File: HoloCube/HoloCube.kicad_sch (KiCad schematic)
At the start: 38 parts, among them J1 ESPProgUART_RX, J2 Conn_01x08_MountingPin, J3 USB_C_Receptacle_USB2.0, J4 Micro_SD_Card, Q1 MMBT3904, U1 ESP32-PICO-D4, U2 LIS2DH12TR, U3 BH1750FVI-TR, U4 XC6209

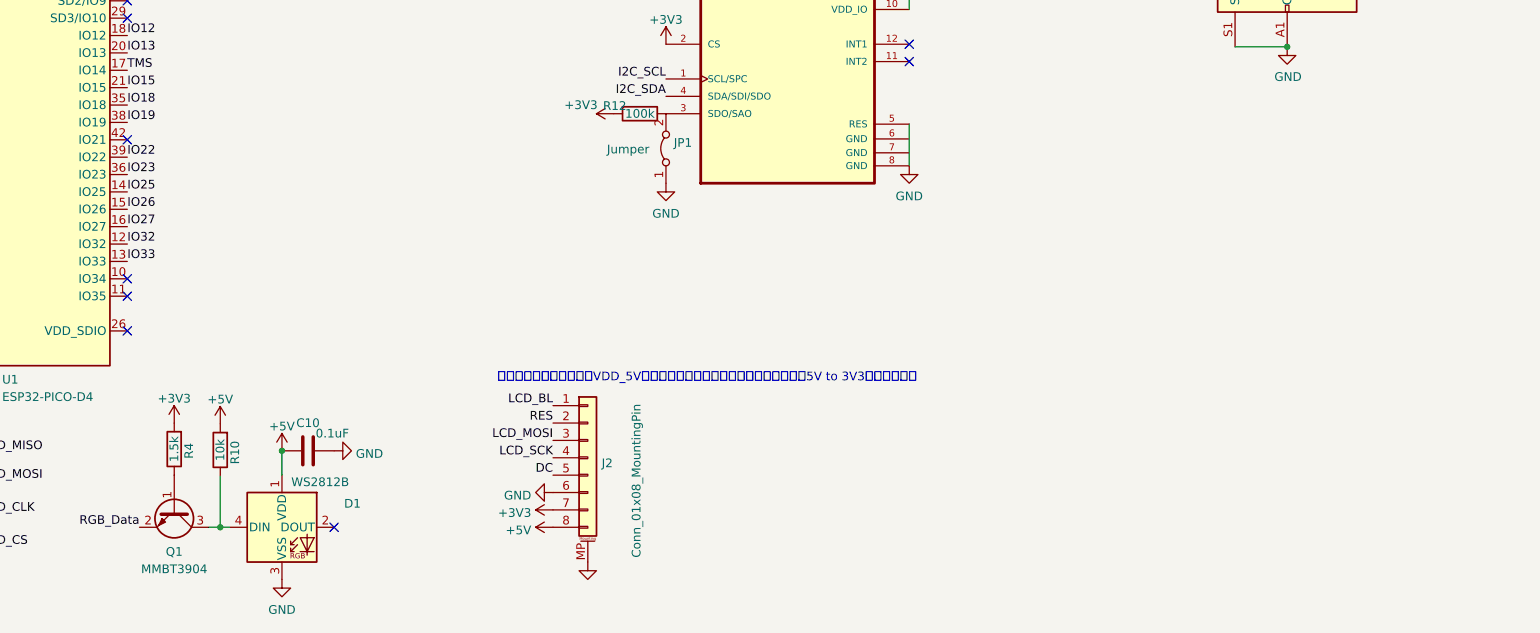
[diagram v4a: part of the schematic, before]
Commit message: 只用三轴还是不方便输入，考虑增加波轮
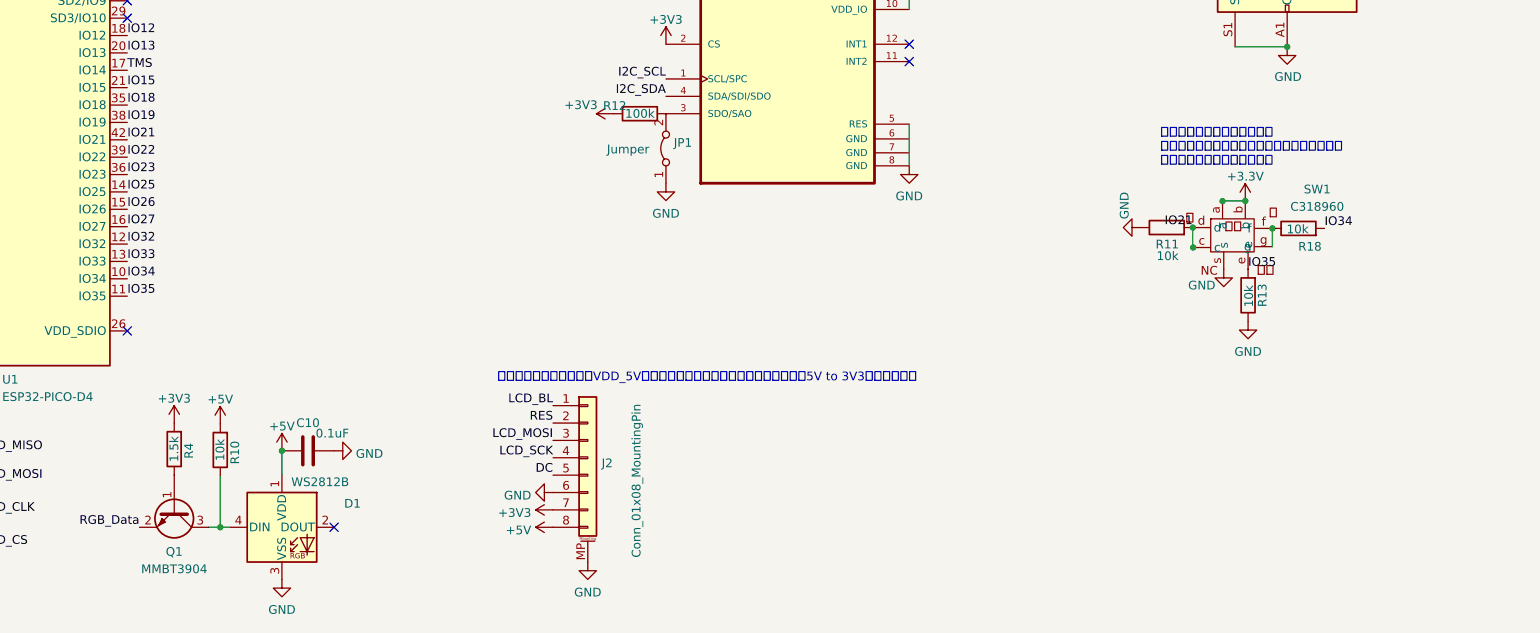
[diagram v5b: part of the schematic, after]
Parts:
- added R11, R13, R18: 10k, Resistor_SMD:R_0402_1005Metric, symbol Device:R
- added SW1: C318960, KisonNew:C318960, symbol KisonNew:C318960
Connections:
- net +3V3: now also SW1.a, SW1.b
- net GND: now also R11.1, R13.1, SW1.s
- net IO34: now reaches U1.10 (IO34)
- net IO34: now also R18.2
- net IO35: now reaches U1.11 (IO35)
- net IO35: now also R13.2, SW1.e
- net IO21: now reaches U1.42 (IO21)
- net IO21: now also SW1.c
- new net: R11.2, SW1.d
- new net: R18.1, SW1.f, SW1.g
- no-connect marks 28 -> 25
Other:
- note added: "这个太丑了，得弄好看一点。 另外如果主板放不下考虑放到屏幕那块板子上？ 其实就应该直接放在屏幕板上"

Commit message: Fix  Error & add SW
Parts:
- removed J2: Conn_01x08_MountingPin, Connector_FFC-FPC:TE_0-1734839-8_1x08-1MP_P0.5mm_Horizontal, symbol Connector_Generic_MountingPin:Conn_01x08_MountingPin
- removed R11, R13, R18: 10k, Resistor_SMD:R_0402_1005Metric, symbol Device:R
- removed R2: 0, Resistor_SMD:R_0402_1005Metric, symbol Device:R
- removed SW1: C318960, KisonNew:C318960, symbol KisonNew:C318960
- added J2: Conn_01x12_MountingPin, Connector_FFC-FPC:Hirose_FH12-12S-0.5SH_1x12-1MP_P0.50mm_Horizontal, symbol Connector_Generic_MountingPin:Conn_01x12_MountingPin
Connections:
- net +3V3: now also J1.2 (VDD), J2.7 (Pin_7)
- net +5V: now also J2.8 (Pin_8)
- net DC: now also J2.5 (Pin_5)
- net GND: now also U2.6 (GND), U2.7 (GND), J2.12 (Pin_12), J2.6 (Pin_6), J2.MP (MountPin)
- net IO18: now also J2.4 (Pin_4)
- net IO22: now also J2.1 (Pin_1)
- net IO4: now also J2.2 (Pin_2)
- net IO5: now also J2.3 (Pin_3)
- net IO12: no longer names the net of U1.18 (IO12)
- net IO21 renamed BTN_Down
- net BTN_Down: now also J2.11 (Pin_11)
- net IO27 renamed BTN_Right
- net BTN_Right: now also J2.9 (Pin_9)
- net TMS renamed BTN_Left
- net BTN_Left: now also J2.10 (Pin_10)
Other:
- note removed: "智慧君的扩展板上，这个VDD_5V其实没用到，可以考虑扩展板上放个额外的5V to 3V3继续降低发热"
- note removed: "这个太丑了，得弄好看一点。 另外如果主板放不下考虑放到屏幕那块板子上？ 其实就应该直接放在屏幕板上"

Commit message: 投板版本
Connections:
- net IO34: no longer names the net of U1.10 (IO34)
- net IO35: no longer names the net of U1.11 (IO35)
- no-connect marks 25 -> 28
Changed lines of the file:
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@@
   (junction (at 45.085 164.084) (diameter 0) (color 0 0 0 0)
   )
+  (no_connect (at 72.898 138.684))
+  (no_connect (at 72.898 141.224))
   (no_connect (at 72.898 98.044))
   (no_connect (at 72.898 100.584))
@@
   (no_connect (at 187.198 104.394))
   (no_connect (at 187.198 106.934))
+  (no_connect (at 72.898 103.124))
   (no_connect (at 103.124 175.006))
   (no_connect (at 228.473 41.148))
@@
     (effects (font (size 1.27 1.27)) (justify left bottom))
   )
-  (label "IO35" (at 72.898 141.224 0)
-    (effects (font (size 1.27 1.27)) (justify left bottom))
-  )
   (label "DC" (at 26.924 173.736 0)
     (effects (font (size 1.27 1.27)) (justify left bottom))
@@
     (effects (font (size 1.27 1.27)) (justify left bottom))
   )
-  (label "IO34" (at 72.898 138.684 0)
-    (effects (font (size 1.27 1.27)) (justify left bottom))
-  )

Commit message: Fix most 3D parts
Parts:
- J2: footprint Connector_FFC-FPC:Hirose_FH12-12S-0.5SH_1x12-1MP_P0.50mm_Horizontal -> KisonNew:Hirose_FH12-12S-0.5SH_1x12-1MP_P0.50mm_Horizontal
- J3: footprint Connector_USB:USB_C_Receptacle_HRO_TYPE-C-31-M-12 -> KisonNew:USB_C_Receptacle_HRO_TYPE-C-31-M-12
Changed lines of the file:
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@@
       (effects (font (size 1.27 1.27)) (justify left))
     )
-    (property "Footprint" "Connector_FFC-FPC:Hirose_FH12-12S-0.5SH_1x12-1MP_P0.50mm_Horizontal" (id 2) (at 149.352 155.956 0)
+    (property "Footprint" "KisonNew:Hirose_FH12-12S-0.5SH_1x12-1MP_P0.50mm_Horizontal" (id 2) (at 149.352 155.956 0)
       (effects (font (size 1.27 1.27)) hide)
     )
@@
     (property "Reference" "J3" (id 0) (at 245.1608 59.8932 0))
     (property "Value" "USB_C_Receptacle_USB2.0" (id 1) (at 244.729 62.484 0))
-    (property "Footprint" "Connector_USB:USB_C_Receptacle_HRO_TYPE-C-31-M-12" (id 2) (at 246.253 81.915 0)
+    (property "Footprint" "KisonNew:USB_C_Receptacle_HRO_TYPE-C-31-M-12" (id 2) (at 246.253 81.915 0)
       (effects (font (size 1.27 1.27)) hide)
     )
@@
     )
     (path "/504ab751-c266-4390-ae52-5fa7e3b19b10"
-      (reference "J2") (unit 1) (value "Conn_01x12_MountingPin") (footprint "Connector_FFC-FPC:Hirose_FH12-12S-0.5SH_1x12-1MP_P0.50mm_Horizontal")
+      (reference "J2") (unit 1) (value "Conn_01x12_MountingPin") (footprint "KisonNew:Hirose_FH12-12S-0.5SH_1x12-1MP_P0.50mm_Horizontal")
     )
     (path "/f15eb5af-b449-4723-9151-8d0ef904f670"
-      (reference "J3") (unit 1) (value "USB_C_Receptacle_USB2.0") (footprint "Connector_USB:USB_C_Receptacle_HRO_TYPE-C-31-M-12")
+      (reference "J3") (unit 1) (value "USB_C_Receptacle_USB2.0") (footprint "KisonNew:USB_C_Receptacle_HRO_TYPE-C-31-M-12")
     )
     (path "/0dd6e263-899e-4549-8e45-af474db9b325"
